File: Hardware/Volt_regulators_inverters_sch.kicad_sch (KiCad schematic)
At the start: 14 parts, among them U11 LM2665M6, U6 TPS73133DBV, U7 TPS72325DBV, U8 TLV70310DBVR

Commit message: Add final changes
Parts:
- C25: value 0.1uF -> 0.1 uF; footprint Capacitor_SMD:C_0603_1608Metric -> Capacitor_SMD:C_0402_1005Metric
- C44, C45, C46: footprint Capacitor_SMD:C_0603_1608Metric -> Capacitor_SMD:C_0402_1005Metric
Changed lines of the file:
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@@
 			)
 		)
-		(property "Footprint" "Capacitor_SMD:C_0603_1608Metric"
+		(property "Footprint" "Capacitor_SMD:C_0402_1005Metric"
 			(at 76.2 123.19 0)
 			(effects
@@
 			)
 		)
-		(property "Footprint" "Capacitor_SMD:C_0603_1608Metric"
+		(property "Footprint" "Capacitor_SMD:C_0402_1005Metric"
 			(at 78.74 43.18 0)
 			(effects
@@
 			)
 		)
-		(property "Footprint" "Capacitor_SMD:C_0603_1608Metric"
+		(property "Footprint" "Capacitor_SMD:C_0402_1005Metric"
 			(at 90.17 43.18 0)
 			(effects
@@
 			)
 		)
-		(property "Value" "0.1uF"
+		(property "Value" "0.1 uF"
 			(at 38.1 167.6335 0)
 			(effects
@@
 			)
 		)
-		(property "Footprint" "Capacitor_SMD:C_0603_1608Metric"
+		(property "Footprint" "Capacitor_SMD:C_0402_1005Metric"
 			(at 35.56 166.37 0)
 			(effects

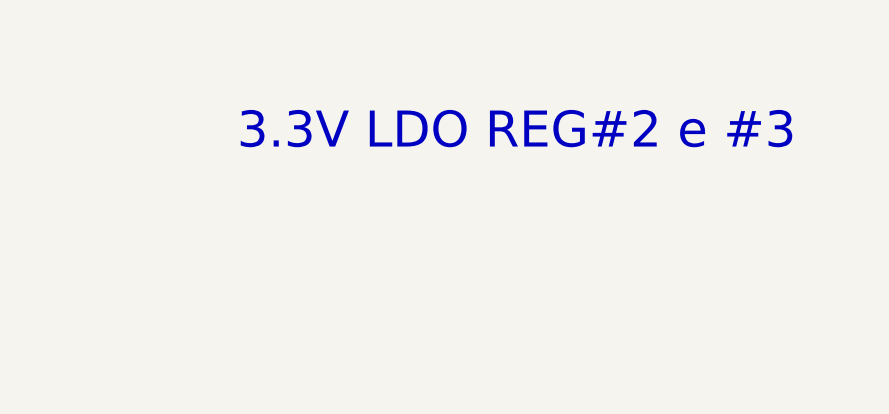
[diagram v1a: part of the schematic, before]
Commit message: feat: add preview images
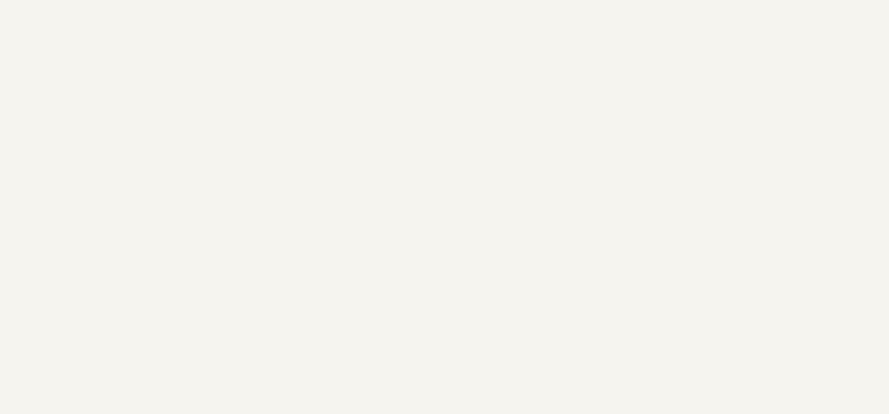
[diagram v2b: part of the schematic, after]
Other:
- note removed: "3.3V LDO REG#2 e #3"
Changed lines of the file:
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@@
-		)
-	)
-	(text "3.3V LDO REG#2 e #3\n\n\n"
-		(exclude_from_sim no)
-		(at 167.386 33.528 0)
-		(effects
-			(font
-				(size 4 4)
-			)
 		)
 	)
